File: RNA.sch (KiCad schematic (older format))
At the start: 81 parts, among them J1 USB_C_Receptacle_USB2.0, J2 AudioJack4, J3 Conn_01x06, SW11 SW_Push_45deg, SW12 SW_Push_45deg, SW13 SW_Push_45deg, SW14 SW_Push_45deg, SW15 SW_Push_45deg, SW16 SW_Push_45deg, SW21 SW_Push_45deg, SW22 SW_Push_45deg, SW23 SW_Push_45deg, SW24 SW_Push_45deg, SW25 SW_Push_45deg, SW26 SW_Push_45deg, SW31 SW_Push_45deg, SW32 SW_Push_45deg, SW33 SW_Push_45deg, SW34 SW_Push_45deg, SW35 SW_Push_45deg, SW36 SW_Push_45deg, SW41 SW_Push_45deg, SW42 SW_Push_45deg, SW43 SW_Push_45deg, SW44 SW_Push_45deg, SW45 SW_Push_45deg, SW46 SW_Push_45deg, SW47 SW_Push_45deg, SW51 SW_Push_45deg, SW52 SW_Push_45deg, SW53 SW_Push_45deg, SW54 SW_Push_45deg, SW55 SW_Push_45deg, SW56 SW_Push_45deg, SW57 SW_Push_45deg

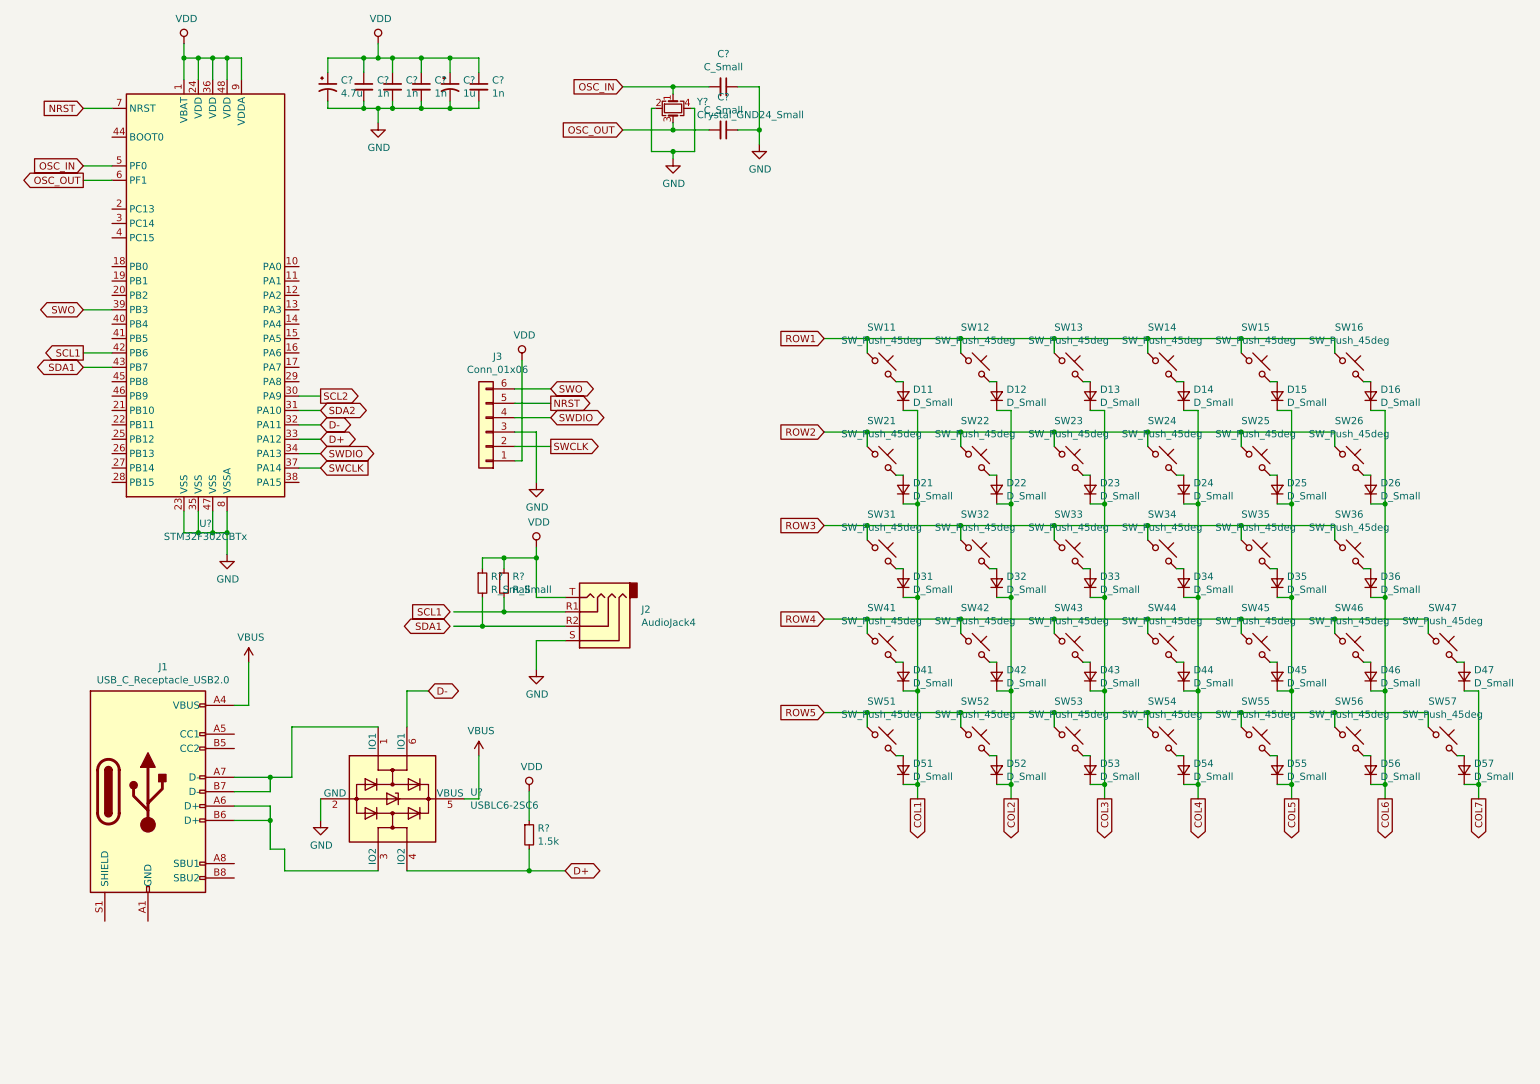
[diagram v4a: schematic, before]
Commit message: add usb reset circuit
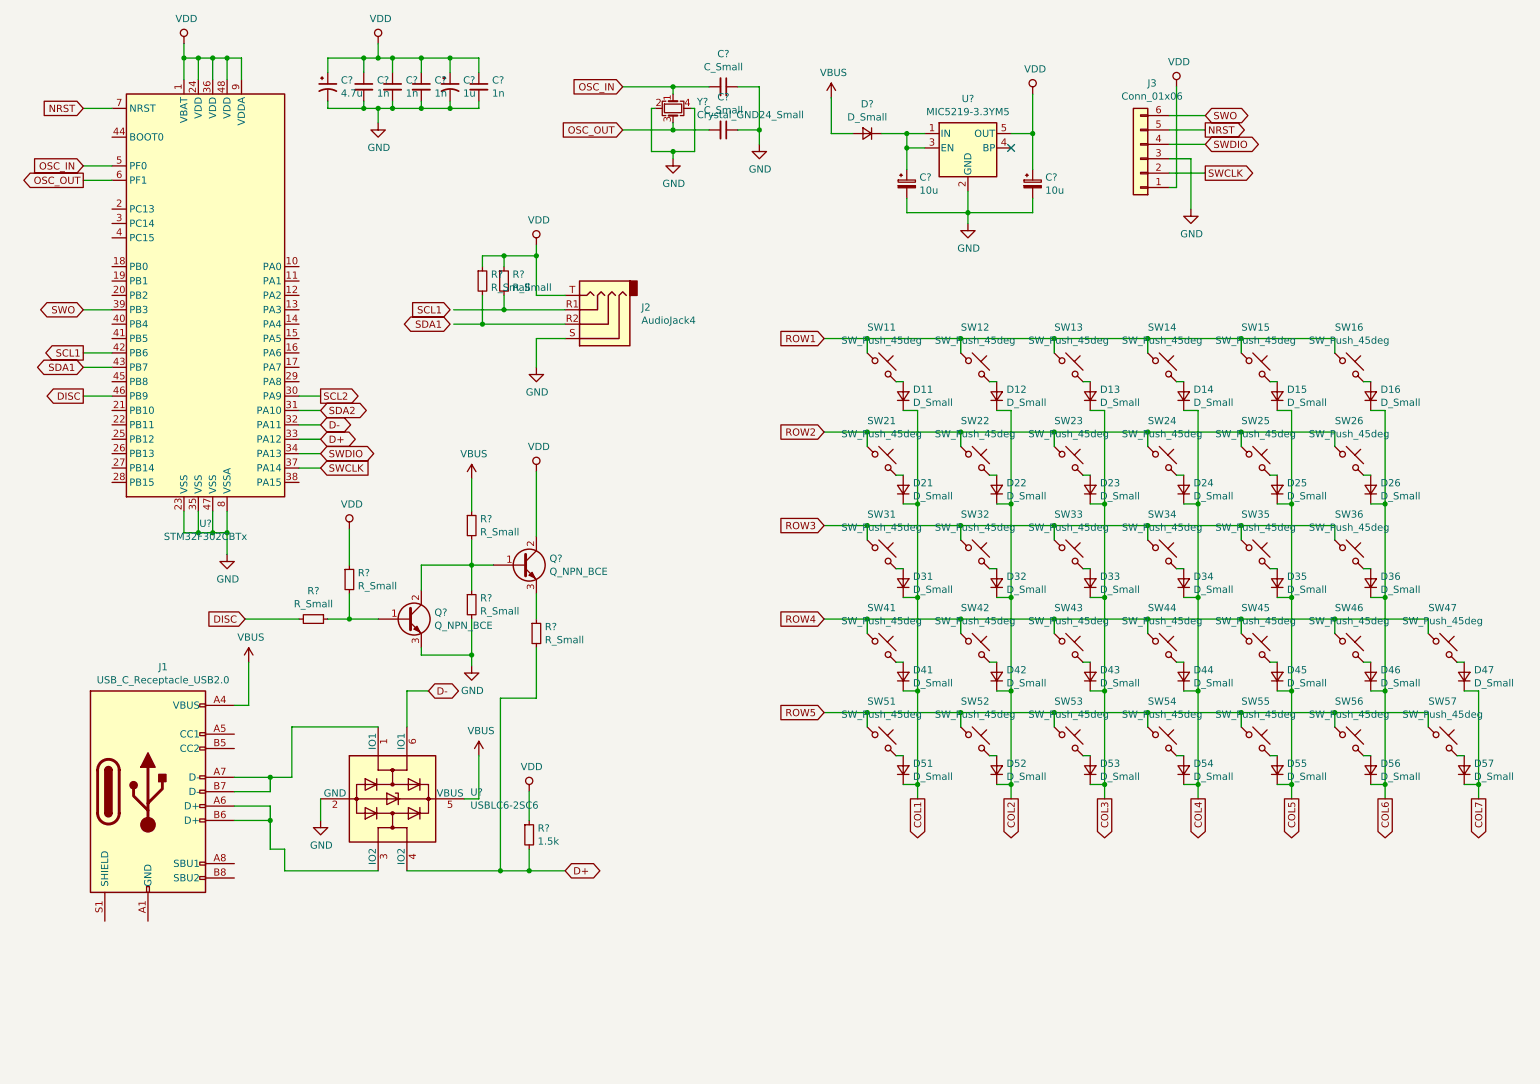
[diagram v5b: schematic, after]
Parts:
- added C? (x2): 10u, symbol Device:CP_Small
- added D?: D_Small, symbol Device:D_Small
- added Q? (x2): Q_NPN_BCE, symbol Device:Q_NPN_BCE
- added R? (x5): R_Small, symbol Device:R_Small
- added U?: MIC5219-3.3YM5, Package_TO_SOT_SMD:SOT-23-5, symbol Regulator_Linear:MIC5219-3.3YM5
- Y?: footprint (none) -> Crystal:Crystal_SMD_5032-4Pin_5.0x3.2mm
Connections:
- net D+: now also R?.2
- net GND: now also C?.2, C?.2, Q?.3 (E), R?.2, U?.2 (GND)
- net VBUS: now also D?.2 (A), R?.1
- net VDD: now also C?.1, Q?.2 (C), R?.1, U?.5 (OUT)
- net DISC: now reaches U?.46 (PB9)
- net DISC: now also R?.2
- new net: C?.1, D?.1 (K), U?.1 (IN), U?.3 (EN)
- new net: Q?.1 (B), Q?.2 (C), R?.1, R?.2
- new net: Q?.3 (E), R?.1
- new net: Q?.1 (B), R?.1, R?.2
- no-connect marks 0 -> 1
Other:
- moved on the sheet: J2, J3, R?

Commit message: add pcb
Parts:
- removed C? (x2): C_Small, Capacitor_SMD:C_0603_1608Metric_Pad1.05x0.95mm_HandSolder, symbol Device:C_Small
- removed J1: USB_C_Receptacle_USB2.0, symbol Connector:USB_C_Receptacle_USB2.0
- removed Q? (x2): Q_NPN_BCE, symbol Device:Q_NPN_BCE
- removed R?: 1.5k, Resistor_SMD:R_0603_1608Metric_Pad1.05x0.95mm_HandSolder, symbol Device:R_Small
- removed R? (x5): R_Small, symbol Device:R_Small
- removed U?: STM32F302CBTx, Package_QFP:LQFP-48_7x7mm_P0.5mm, symbol MCU_ST_STM32F3:STM32F302CBTx
- removed Y?: Crystal_GND24_Small, Crystal:Crystal_SMD_5032-4Pin_5.0x3.2mm, symbol Device:Crystal_GND24_Small
- added C7: C_Small, Capacitor_SMD:C_0603_1608Metric, symbol Device:C_Small
- added F1: 500mA, Fuse:Fuse_1206_3216Metric, symbol Device:Polyfuse_Small
- added J1: USB_B_Micro, Connector_USB:USB_Micro-B_Molex-105017-0001, symbol Connector:USB_B_Micro
- added R3: 10k, Resistor_SMD:R_0603_1608Metric, symbol Device:R_Small
- added SW1, SW2: SW_Push, Button_Switch_SMD:SW_SPST_TL3342, symbol Switch:SW_Push
- added U1: STM32F072C8Tx, Package_QFP:LQFP-48_7x7mm_P0.5mm, symbol MCU_ST_STM32F0:STM32F072C8Tx
- C1, C5: renamed from C?; footprint (none) -> Capacitor_SMD:C_1206_3216Metric
- C10, C9: renamed from C?; footprint (none) -> Capacitor_SMD:C_1206_3216Metric; symbol Device:CP_Small -> Device:CP1_Small
- C2, C3, C4, C6: renamed from C?; footprint Capacitor_SMD:C_0603_1608Metric_Pad1.05x0.95mm_HandSolder -> Capacitor_SMD:C_0603_1608Metric
- D1: renamed from D?; footprint (none) -> Diode_SMD:D_SOD-123
- J2: footprint (none) -> Connector_Audio:Jack_3.5mm_PJ320E_Horizontal
- R5, R6: renamed from R?; footprint Resistor_SMD:R_0603_1608Metric_Pad1.05x0.95mm_HandSolder -> Resistor_SMD:R_0603_1608Metric
- SW11, SW12, SW13, SW14, SW15, SW16, SW21, SW22, SW23, SW24, SW25, SW26, SW31, SW32, SW33, SW34, SW35, SW36, SW41, SW42, SW43, SW44, SW45, SW46, SW47, SW51, SW52, SW53, SW54, SW55, SW56, SW57: footprint keyswitch:PG1350_socket -> keyswitches:PG1350_socket
- gave numbers to parts that had none: 2
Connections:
- net COL1: now also U1.45 (PB8)
- net COL2: now also U1.46 (PB9)
- net COL3: now also U1.21 (PB10)
- net COL4: now also U1.22 (PB11)
- net COL5: now also U1.25 (PB12)
- net COL6: now also U1.26 (PB13)
- net COL7: now also U1.27 (PB14)
- net D+: now also U1.33 (PA12)
- net D-: now also U1.32 (PA11)
- net GND: now also C7.2, J1.5 (GND), J1.6 (Shield), R3.1, SW2.2, U1.23 (VSS), U1.35 (VSS), U1.47 (VSS), U1.8 (VSSA)
- net NRST: now also C7.1, SW2.1, U1.7 (NRST)
- net ROW1: now also U1.10 (PA0)
- net ROW2: now also U1.11 (PA1)
- net ROW3: now also U1.12 (PA2)
- net ROW4: now also U1.13 (PA3)
- net ROW5: now also U1.14 (PA4)
- net SCL1: now also U1.42 (PB6)
- net SCL2: now also U1.30 (PA9)
- net SDA1: now also U1.43 (PB7)
- net SDA2: now also U1.31 (PA10)
- net SWCLK: now also U1.37 (PA14)
- net SWDIO: now also U1.34 (PA13)
- net VBUS: now also F1.1
- net VDD: now also SW1.1, U1.1 (VBAT), U1.24 (VDD), U1.36 (VDDIO2), U1.48 (VDD), U1.9 (VDDA)
- net at U2.3 (IO2): now also J1.3 (D+)
- net at U2.1 (IO1): now also J1.2 (D-)
- net SWO: no longer names the net of J3.6 (Pin_6)
- new net: F1.2, J1.1 (VBUS)
- new net BOOT0: R3.2, SW1.2, U1.44 (BOOT0)
- no-connect marks 1 -> 3

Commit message: wip"
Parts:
- removed C1: 4.7u, Capacitor_SMD:C_1206_3216Metric, symbol Device:CP1_Small
- removed C10, C9: 10u, Capacitor_SMD:C_1206_3216Metric, symbol Device:CP1_Small
- removed C5: 1u, Capacitor_SMD:C_1206_3216Metric, symbol Device:CP1_Small
- removed D1: D_Small, Diode_SMD:D_SOD-123, symbol Device:D_Small
- removed SW1: SW_Push, Button_Switch_SMD:SW_SPST_TL3342, symbol Switch:SW_Push
- removed U2: USBLC6-2SC6, Package_TO_SOT_SMD:SOT-23-6, symbol Power_Protection:USBLC6-2SC6
- removed U3: MIC5219-3.3YM5, Package_TO_SOT_SMD:SOT-23-5, symbol Regulator_Linear:MIC5219-3.3YM5
- added C1, C5: 1u, Capacitor_SMD:C_0603_1608Metric, symbol Device:C_Small
- added D1: D_Schottky_Small, Diode_SMD:D_SOD-323, symbol Device:D_Schottky_Small
- added J4: AudioJack4, Connector_PinHeader_2.54mm:PinHeader_1x04_P2.54mm_Vertical, symbol Connector_Generic:Conn_01x04
- added R1, R2: R_Small, Resistor_SMD:R_0603_1608Metric, symbol Device:R_Small
- added R4: 39k, Resistor_SMD:R_0603_1608Metric, symbol Device:R_Small
- added R7: 68k, Resistor_SMD:R_0603_1608Metric, symbol Device:R_Small
- added SW1: SW_SPST, Button_Switch_SMD:SW_DIP_SPSTx01_Slide_6.7x4.1mm_W8.61mm_P2.54mm_LowProfile, symbol Switch:SW_SPST
- added U2: PRTR5V0U2X, random-keyboard-parts:SOT143B, symbol random-keyboard-parts:PRTR5V0U2X
- added U3: MCP1703A-3302_SOT23, Package_TO_SOT_SMD:SOT-23, symbol Regulator_Linear:MCP1703A-3302_SOT23
- C2, C3, C4, C6: value 1n -> 100n
- J2: footprint Connector_Audio:Jack_3.5mm_PJ320E_Horizontal -> Connector_JST:JST_SH_SM04B-SRSS-TB_1x04-1MP_P1.00mm_Horizontal; symbol Connector:AudioJack4 -> Connector_Generic:Conn_01x04
- J3: footprint Connector_PinSocket_2.54mm:PinSocket_1x06_P2.54mm_Vertical -> Connector_PinHeader_2.54mm:PinHeader_2x03_P2.54mm_Vertical
- SW2: footprint Button_Switch_SMD:SW_SPST_TL3342 -> Button_Switch_SMD:Panasonic_EVQPUL_EVQPUC
- U1: symbol MCU_ST_STM32F0:STM32F072C8Tx -> MCU_ST_STM32L4:STM32L433CCTx
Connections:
- net BOOT0: now also U1.5 (PH0), SW1.2 (B); no longer U1.44 (BOOT0)
- net D+: now also J1.3 (D+), U2.2 (IO1)
- net D-: now also J1.2 (D-), U2.3 (IO2)
- net GND: now also J2.4 (Pin_4), C1.2, C5.2, J4.4 (Pin_4), R7.2, U2.1 (GND), U3.1 (GND); no longer J2.S
- net VBUS: now also D1.2 (A), R4.1, U2.4 (VCC)
- net VDD: now also J2.1 (Pin_1), C5.1, J4.1 (Pin_1), R1.1, R2.1, SW1.1 (A), U3.2 (VO); no longer J2.T
- net VBUS_SENSE: now reaches U1.38 (PA15)
- net VBUS_SENSE: now also R4.2, R7.1
- net SWO: now reaches U1.39 (PB3)
- net at R6.2: now also J2.2 (Pin_2); no longer J2.R1
- net at R5.2: now also J2.3 (Pin_3); no longer J2.R2
- new net: J4.2 (Pin_2), R2.2
- new net: J4.3 (Pin_3), R1.2
- new net: C1.1, D1.1 (K), U3.3 (VI)
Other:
- moved on the sheet: R3, R5, R6, U1

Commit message: add sub(right-hand) keyboard
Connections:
- net SCL1: now also J2.2 (Pin_2), R6.2
- net SCL2: now also J4.2 (Pin_2), R2.2
- net SDA1: now also J2.3 (Pin_3), R5.2
- net SDA2: now also J4.3 (Pin_3), R1.2
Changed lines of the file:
@@
 EESchema Schematic File Version 4
 LIBS:RNA-cache
-EELAYER 26 0
+EELAYER 29 0
 EELAYER END
 $Descr A4 11693 8268
 encoding utf-8
-Sheet 1 1
+Sheet 1 2
 Title ""
 Date ""
@@
 Text GLabel 4950 7100 0    50   BiDi ~ 0
 SDA1
-Wire Wire Line
-	4975 7100 5175 7100
 Connection ~ 5175 7100
-Wire Wire Line
-	4975 7000 5325 7000
 Connection ~ 5325 7000
 NoConn ~ 7300 1375
@@
 Text GLabel 4300 5250 0    50   BiDi ~ 0
 SDA2
-Wire Wire Line
-	4325 5250 4525 5250
 Connection ~ 4525 5250
-Wire Wire Line
-	4325 5150 4675 5150
 Connection ~ 4675 5150
 Text GLabel 2500 3700 2    50   Input ~ 0
@@
 Wire Wire Line
 	2500 5350 2500 6150
+Wire Wire Line
+	4300 5250 4525 5250
+Wire Wire Line
+	4300 5150 4675 5150
+Wire Wire Line
+	4950 7100 5175 7100
+Wire Wire Line
+	4950 7000 5325 7000
+$Sheet
+S 1300 6950 1850 750
+U 5D06BBC1
+F0 "RNA_SubBoard" 50
+F1 "RNA_Sub.sch" 50
+$EndSheet
 $EndSCHEMATC
